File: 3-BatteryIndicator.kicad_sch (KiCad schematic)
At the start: 11 parts, among them U301 BC847BS,115

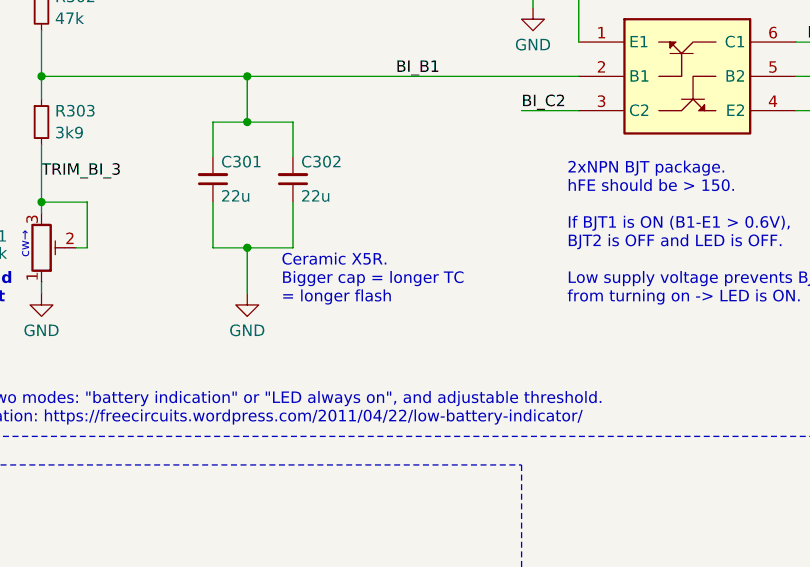
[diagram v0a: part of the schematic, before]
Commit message: fixing missing DC jack; continued working on the board layout
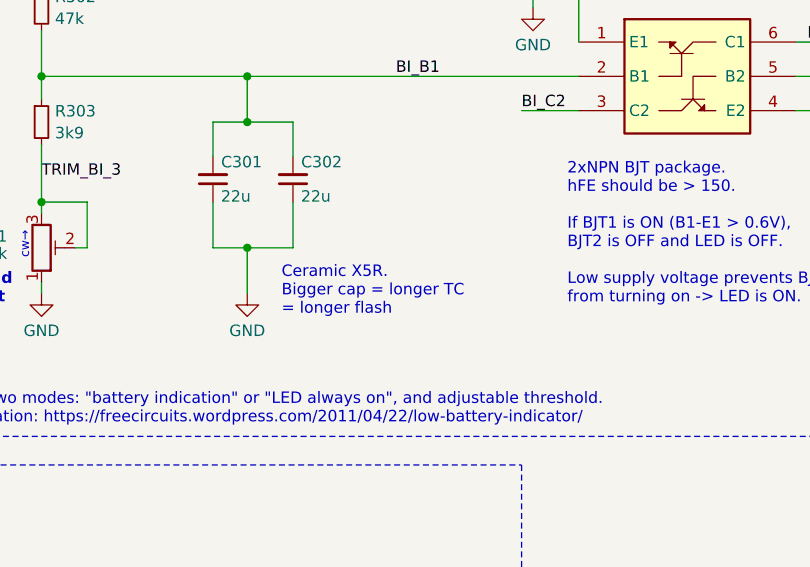
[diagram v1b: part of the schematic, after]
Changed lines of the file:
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@@
 	(text "Ceramic X5R.\nBigger cap = longer TC\n= longer flash"
 		(exclude_from_sim no)
-		(at 116.84 115.57 0)
+		(at 116.84 116.84 0)
 		(effects
 			(font

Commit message: schematic: finishing standoffs, screws, minor improvements
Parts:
- S301: Source Mouser -> TME
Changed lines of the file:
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@@
 		)
 		(instances
-			(project "2023_PiezoPreamp"
+			(project "2024_PiezoPreamp3"
 				(path "/6e141482-2809-49ad-b316-4cdedc98ad26/92c2a844-101a-40c5-a0eb-d2ce1ffb9165"
 					(reference "D301")
@@
 		)
 		(instances
-			(project "2023_PiezoPreamp"
+			(project "2024_PiezoPreamp3"
 				(path "/6e141482-2809-49ad-b316-4cdedc98ad26/92c2a844-101a-40c5-a0eb-d2ce1ffb9165"
 					(reference "#PWR09")
@@
 		)
 		(instances
-			(project "2023_PiezoPreamp"
+			(project "2024_PiezoPreamp3"
 				(path "/6e141482-2809-49ad-b316-4cdedc98ad26/92c2a844-101a-40c5-a0eb-d2ce1ffb9165"
 					(reference "C302")
@@
 		)
 		(instances
-			(project "2023_PiezoPreamp"
+			(project "2024_PiezoPreamp3"
 				(path "/6e141482-2809-49ad-b316-4cdedc98ad26/92c2a844-101a-40c5-a0eb-d2ce1ffb9165"
 					(reference "R305")
@@
 		)
 		(instances
-			(project "2023_PiezoPreamp"
+			(project "2024_PiezoPreamp3"
 				(path "/6e141482-2809-49ad-b316-4cdedc98ad26/92c2a844-101a-40c5-a0eb-d2ce1ffb9165"
 					(reference "#PWR05")
@@
 		)
 		(instances
-			(project "2023_PiezoPreamp"
+			(project "2024_PiezoPreamp3"
 				(path "/6e141482-2809-49ad-b316-4cdedc98ad26/92c2a844-101a-40c5-a0eb-d2ce1ffb9165"
 					(reference "C301")
@@
 		)
 		(instances
-			(project "2023_PiezoPreamp"
+			(project "2024_PiezoPreamp3"
 				(path "/6e141482-2809-49ad-b316-4cdedc98ad26/92c2a844-101a-40c5-a0eb-d2ce1ffb9165"
 					(reference "#PWR012")
@@
 		)
 		(instances
-			(project "2023_PiezoPreamp"
+			(project "2024_PiezoPreamp3"
 				(path "/6e141482-2809-49ad-b316-4cdedc98ad26/92c2a844-101a-40c5-a0eb-d2ce1ffb9165"
 					(reference "U301")
@@
 		)
 		(instances
-			(project "2023_PiezoPreamp"
+			(project "2024_PiezoPreamp3"
 				(path "/6e141482-2809-49ad-b316-4cdedc98ad26/92c2a844-101a-40c5-a0eb-d2ce1ffb9165"
 					(reference "R301")
@@
 		)
 		(instances
-			(project "2023_PiezoPreamp"
+			(project "2024_PiezoPreamp3"
 				(path "/6e141482-2809-49ad-b316-4cdedc98ad26/92c2a844-101a-40c5-a0eb-d2ce1ffb9165"
 					(reference "#PWR013")
@@
 		)
 		(instances
-			(project "2023_PiezoPreamp"
+			(project "2024_PiezoPreamp3"
 				(path "/6e141482-2809-49ad-b316-4cdedc98ad26/92c2a844-101a-40c5-a0eb-d2ce1ffb9165"
 					(reference "RV301")
@@
 		)
 		(instances
-			(project "2023_PiezoPreamp"
+			(project "2024_PiezoPreamp3"
 				(path "/6e141482-2809-49ad-b316-4cdedc98ad26/92c2a844-101a-40c5-a0eb-d2ce1ffb9165"
 					(reference "R303")
@@
 		)
 		(instances
-			(project "2023_PiezoPreamp"
+			(project "2024_PiezoPreamp3"
 				(path "/6e141482-2809-49ad-b316-4cdedc98ad26/92c2a844-101a-40c5-a0eb-d2ce1ffb9165"
 					(reference "R302")
@@
 		)
 		(instances
-			(project "2023_PiezoPreamp"
+			(project "2024_PiezoPreamp3"
 				(path "/6e141482-2809-49ad-b316-4cdedc98ad26/92c2a844-101a-40c5-a0eb-d2ce1ffb9165"
 					(reference "R304")
@@
 			)
 		)
-		(property "Source" "Mouser"
+		(property "Source" "TME"
 			(at 66.04 151.13 0)
 			(effects
@@
 		)
 		(instances
-			(project "2023_PiezoPreamp"
+			(project "2024_PiezoPreamp3"
 				(path "/6e141482-2809-49ad-b316-4cdedc98ad26/92c2a844-101a-40c5-a0eb-d2ce1ffb9165"
 					(reference "S301")

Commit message: Schematics: improving Purpose of some components
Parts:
- S301: Purpose changes the mode of power-on LED. Left = BI, right = LED al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 -> SPDT. Changes the mode of power-on LED. Left = BI, right = 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
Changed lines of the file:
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@@
 			)
 		)
-		(property "Purpose" "changes the mode of power-on LED. Left = BI, right = LED always on"
+		(property "Purpose" "SPDT. Changes the mode of power-on LED. Left = BI, right = LED always on"
 			(at 66.04 151.13 0)
 			(effects
